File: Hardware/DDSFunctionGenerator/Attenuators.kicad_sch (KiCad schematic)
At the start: 30 parts, among them J1 Conn_Coaxial, Q1 Q_NPN_BEC, Q2 Q_NPN_BEC, Q3 Q_NPN_BEC

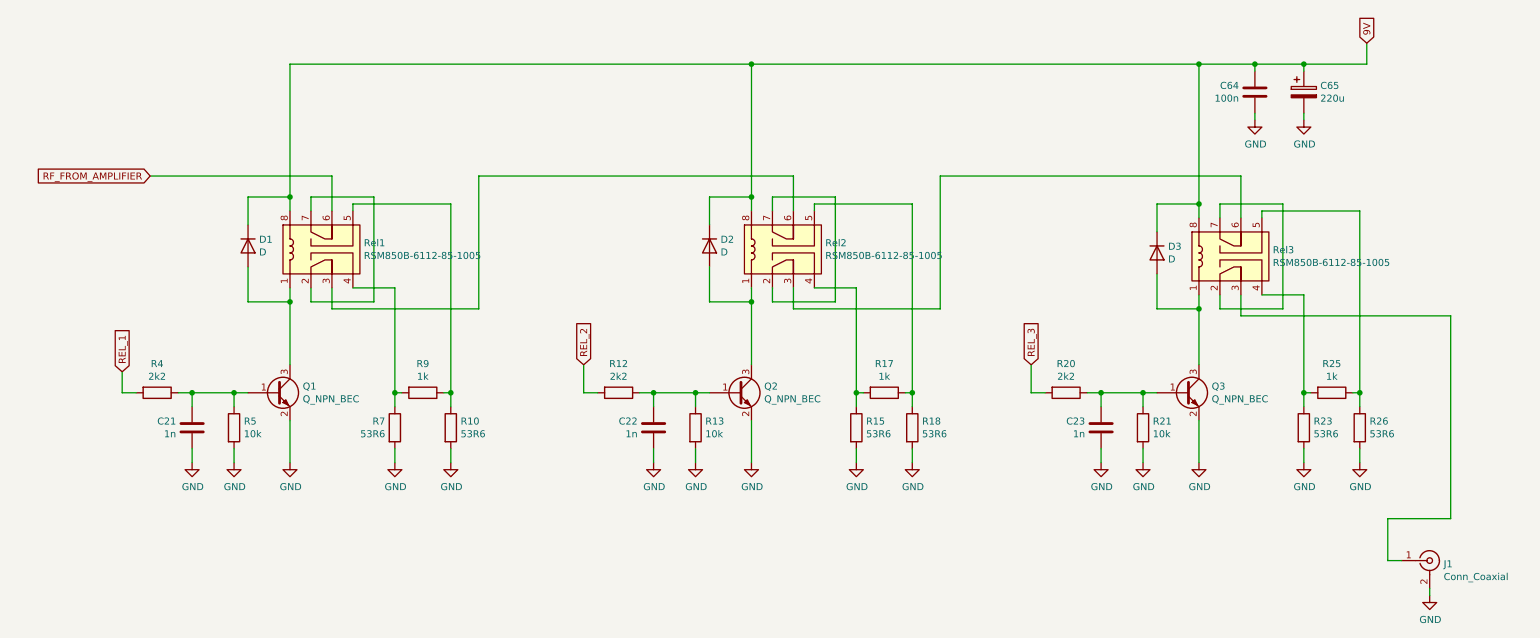
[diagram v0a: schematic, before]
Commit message: move to raspbbery pico, first draft
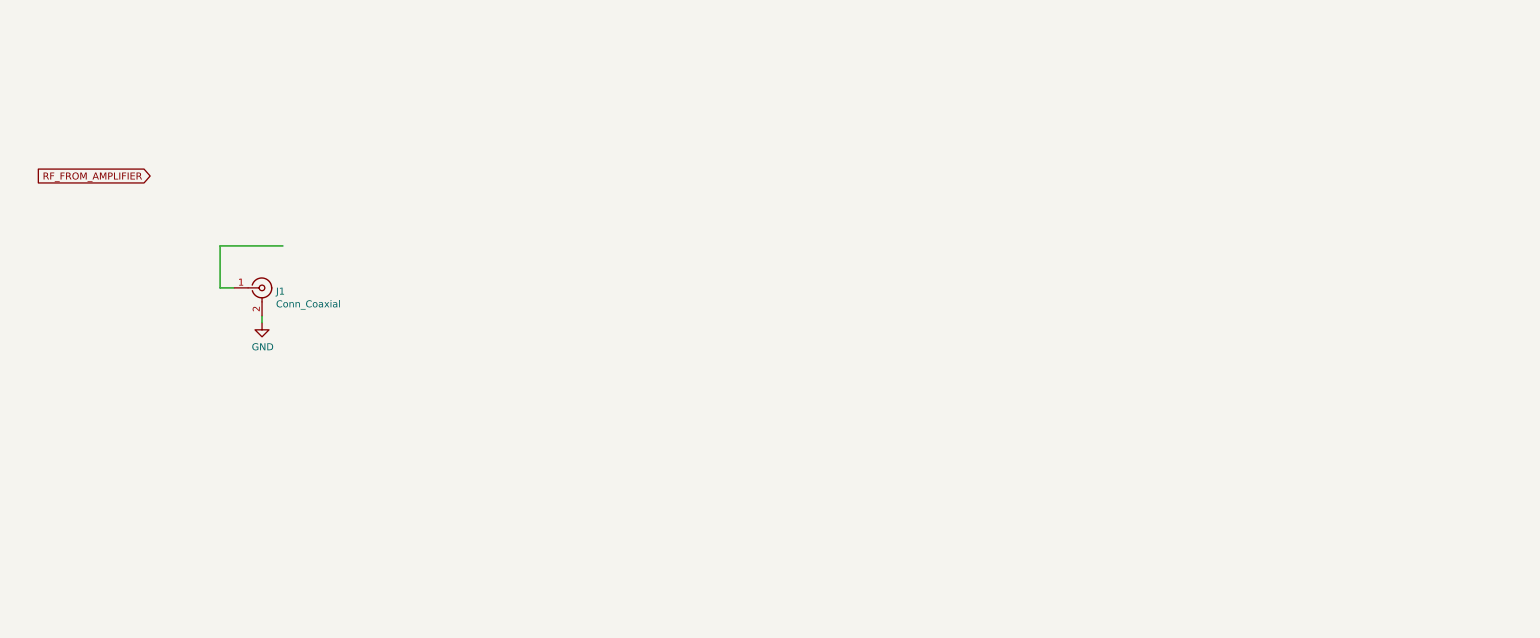
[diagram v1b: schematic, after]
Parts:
- removed C21, C22, C23: 1n, Capacitor_SMD:C_0402_1005Metric, symbol Device:C
- removed C64: 100n, Capacitor_SMD:C_0402_1005Metric, symbol Device:C
- removed C65: 220u, Capacitor_SMD:CP_Elec_6.3x5.8, symbol Device:CP
- removed D1, D2, D3: D, Diode_SMD:D_MiniMELF, symbol Device:D
- removed Q1, Q2, Q3: Q_NPN_BEC, Package_TO_SOT_SMD:SOT-323_SC-70, symbol Device:Q_NPN_BEC
- removed R10, R15, R18, R23, R26, R7: 53R6, Resistor_SMD:R_0402_1005Metric, symbol Device:R
- removed R12, R20, R4: 2k2, Resistor_SMD:R_0402_1005Metric, symbol Device:R
- removed R13, R21, R5: 10k, Resistor_SMD:R_0402_1005Metric, symbol Device:R
- removed R17, R25, R9: 1k, Resistor_SMD:R_0402_1005Metric, symbol Device:R
- removed Rel1, Rel2, Rel3: RSM850B-6112-85-1005, Relay_THT:Relay_DPDT_Omron_G6K-2P-Y, symbol NumericallyControlledOscillator:RSM850B-6112-85-1005
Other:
- moved on the sheet: J1
